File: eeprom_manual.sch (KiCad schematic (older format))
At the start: 45 parts, among them J1 Barrel_Jack, J2 Conn_01x02, SW1 SW_SPST, SW2 SW_DIP_x08, SW3 SW_DIP_x10, SW4 SW_DIP_x01, U1 74HC245, U2 L7805, U4 M54513FP, U5 28C16

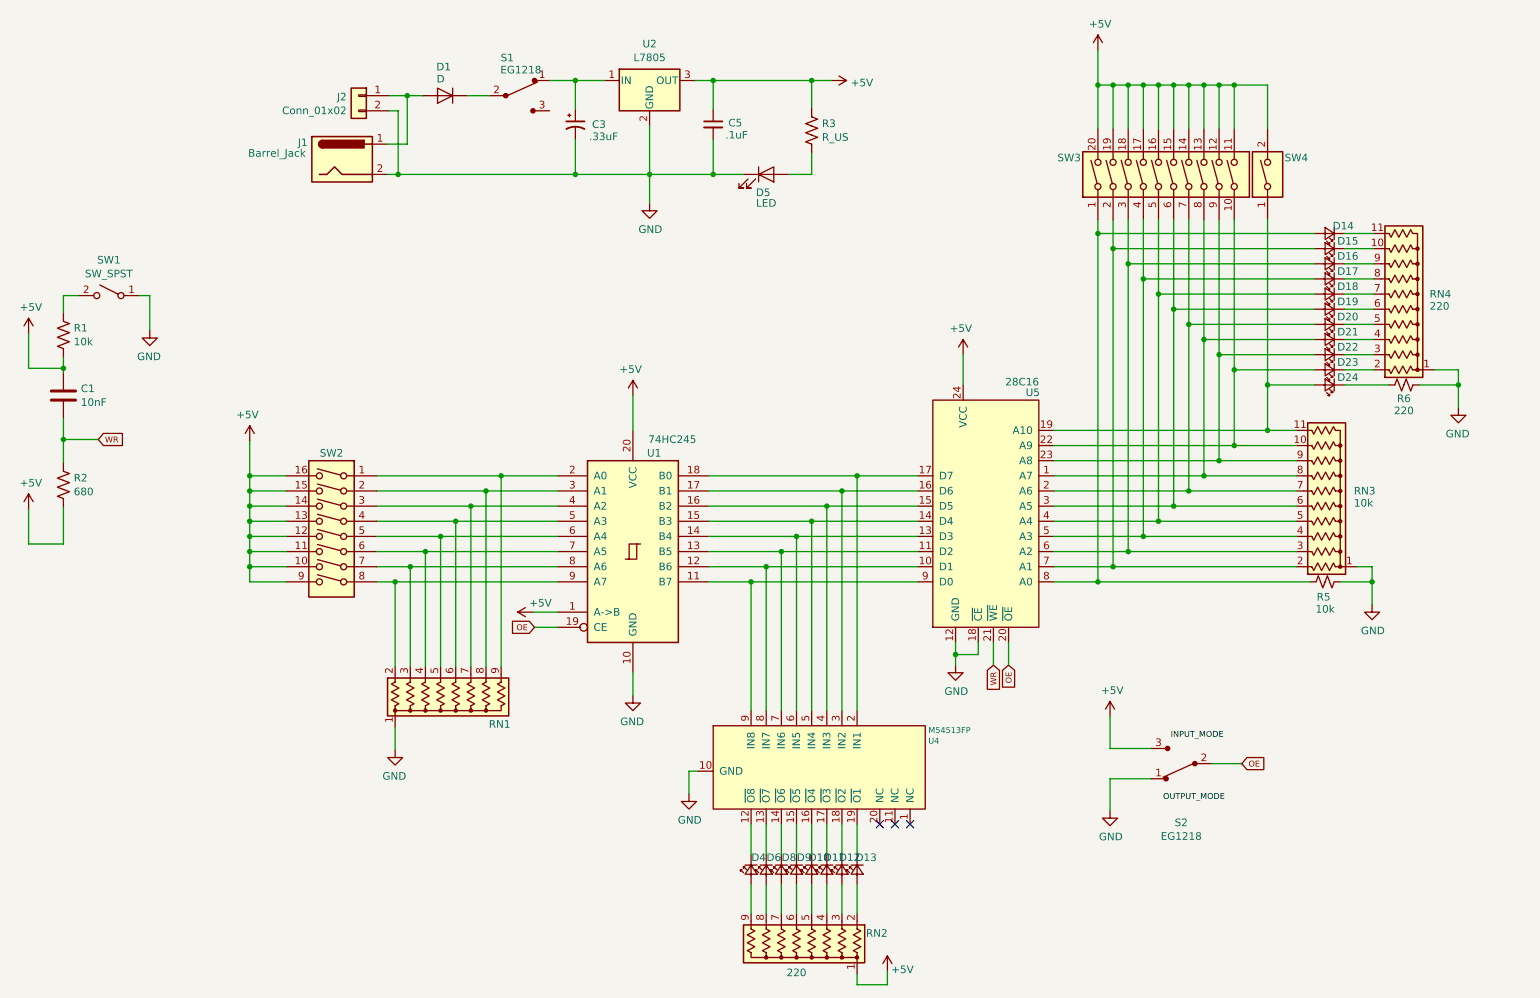
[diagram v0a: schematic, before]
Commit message: Assign footprints (initial)
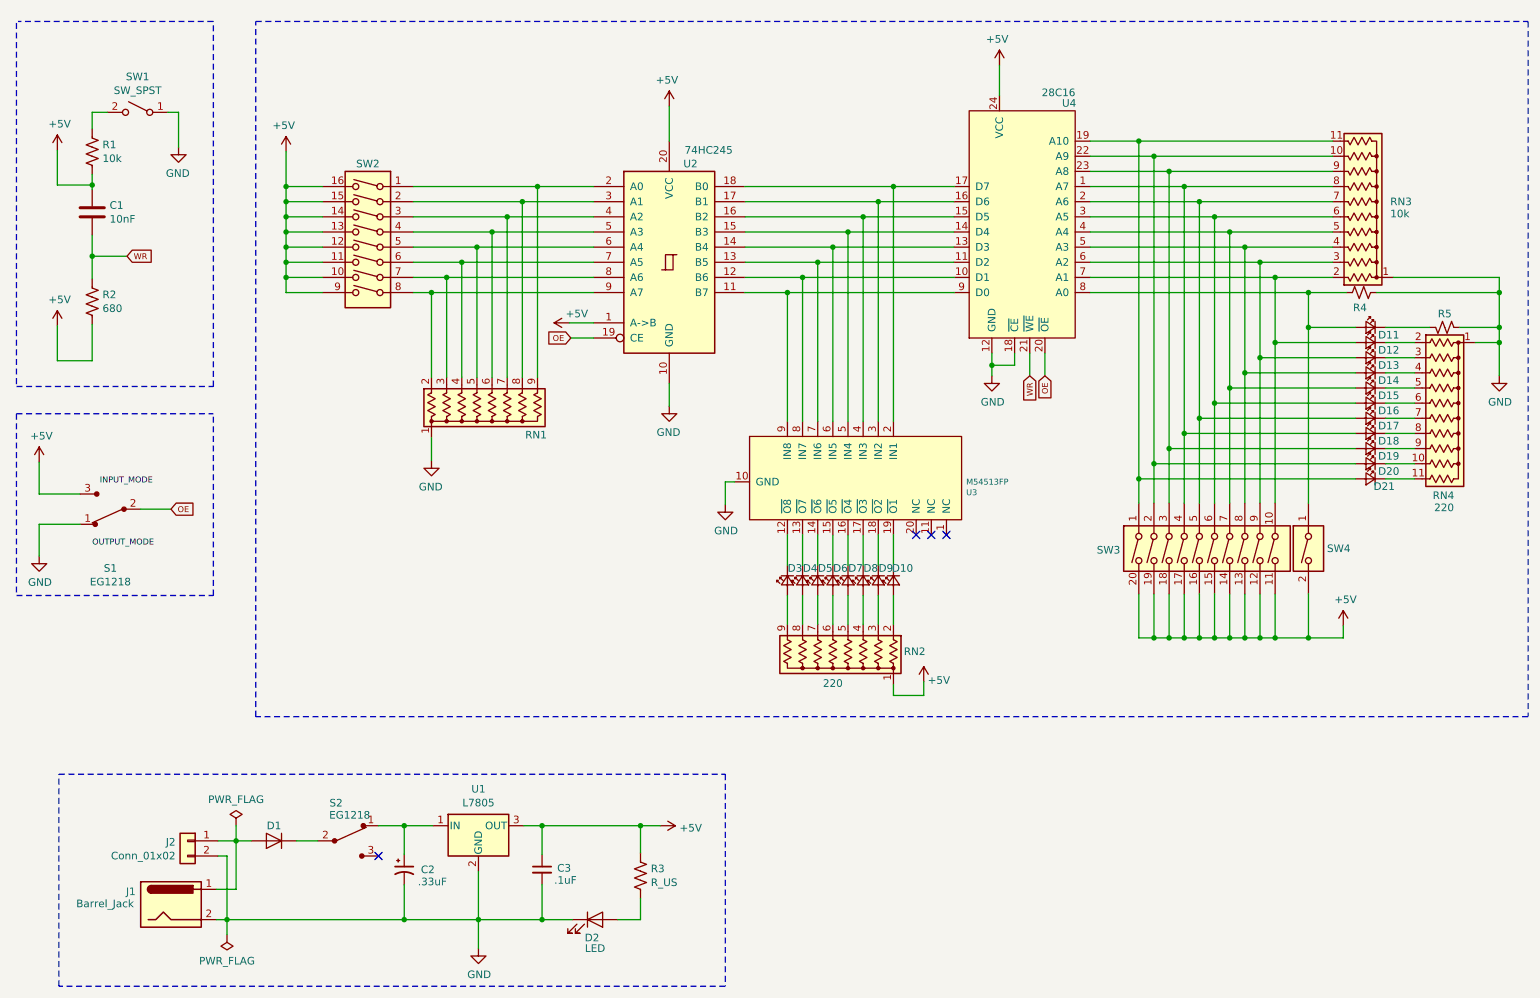
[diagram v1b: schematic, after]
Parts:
- C1: footprint (none) -> Capacitor_SMD:C_0805_2012Metric_Pad1.15x1.40mm_HandSolder
- C2: renamed from C3; footprint (none) -> Capacitor_SMD:C_0805_2012Metric_Pad1.15x1.40mm_HandSolder
- C3: renamed from C5; footprint (none) -> Capacitor_SMD:C_0805_2012Metric_Pad1.15x1.40mm_HandSolder
- D1: footprint (none) -> Diode_SMD:D_0805_2012Metric_Pad1.15x1.40mm_HandSolder
- D10: renamed from D13; footprint (none) -> LED_SMD:LED_0805_2012Metric_Pad1.15x1.40mm_HandSolder
- D11: renamed from D24; footprint (none) -> LED_SMD:LED_0805_2012Metric_Pad1.15x1.40mm_HandSolder
- D12: renamed from D23; footprint (none) -> LED_SMD:LED_0805_2012Metric_Pad1.15x1.40mm_HandSolder
- D13: renamed from D22; footprint (none) -> LED_SMD:LED_0805_2012Metric_Pad1.15x1.40mm_HandSolder
- D14: renamed from D21; footprint (none) -> LED_SMD:LED_0805_2012Metric_Pad1.15x1.40mm_HandSolder
- D15: renamed from D20; footprint (none) -> LED_SMD:LED_0805_2012Metric_Pad1.15x1.40mm_HandSolder
- D16: renamed from D19; footprint (none) -> LED_SMD:LED_0805_2012Metric_Pad1.15x1.40mm_HandSolder
- D17: renamed from D18; footprint (none) -> LED_SMD:LED_0805_2012Metric_Pad1.15x1.40mm_HandSolder
- D18: renamed from D17; footprint (none) -> LED_SMD:LED_0805_2012Metric_Pad1.15x1.40mm_HandSolder
- D19: renamed from D16; footprint (none) -> LED_SMD:LED_0805_2012Metric_Pad1.15x1.40mm_HandSolder
- D2: renamed from D5; footprint (none) -> LED_SMD:LED_0805_2012Metric_Pad1.15x1.40mm_HandSolder
- D20: renamed from D15; footprint (none) -> LED_SMD:LED_0805_2012Metric_Pad1.15x1.40mm_HandSolder
- D21: renamed from D14; footprint (none) -> LED_SMD:LED_0805_2012Metric_Pad1.15x1.40mm_HandSolder
- D3: renamed from D4; footprint (none) -> LED_SMD:LED_0805_2012Metric_Pad1.15x1.40mm_HandSolder
- D4: renamed from D6; footprint (none) -> LED_SMD:LED_0805_2012Metric_Pad1.15x1.40mm_HandSolder
- D5: renamed from D8; footprint (none) -> LED_SMD:LED_0805_2012Metric_Pad1.15x1.40mm_HandSolder
- D6: renamed from D9; footprint (none) -> LED_SMD:LED_0805_2012Metric_Pad1.15x1.40mm_HandSolder
- D7: renamed from D10; footprint (none) -> LED_SMD:LED_0805_2012Metric_Pad1.15x1.40mm_HandSolder
- D8: renamed from D11; footprint (none) -> LED_SMD:LED_0805_2012Metric_Pad1.15x1.40mm_HandSolder
- D9: renamed from D12; footprint (none) -> LED_SMD:LED_0805_2012Metric_Pad1.15x1.40mm_HandSolder
- J1: footprint (none) -> digikey-footprints:Barrel_Jack_5.5mmODx2.1mmID_PJ-202A
- J2: footprint (none) -> TerminalBlock:TerminalBlock_bornier-2_P5.08mm
- R1, R2, R3: footprint (none) -> Resistor_SMD:R_0805_2012Metric_Pad1.15x1.40mm_HandSolder
- R4: renamed from R5; footprint (none) -> Resistor_SMD:R_0805_2012Metric_Pad1.15x1.40mm_HandSolder
- R5: renamed from R6; footprint (none) -> Resistor_SMD:R_0805_2012Metric_Pad1.15x1.40mm_HandSolder
- SW1: footprint (none) -> Button_Switch_THT:SW_PUSH_6mm
- SW2: footprint (none) -> Button_Switch_THT:SW_DIP_SPSTx08_Slide_9.78x22.5mm_W7.62mm_P2.54mm
- SW3: footprint (none) -> Button_Switch_THT:SW_DIP_SPSTx10_Slide_9.78x27.58mm_W7.62mm_P2.54mm
- SW4: footprint (none) -> Button_Switch_THT:SW_DIP_SPSTx01_Slide_9.78x4.72mm_W7.62mm_P2.54mm
- U1: renamed from U2; footprint (none) -> Package_TO_SOT_THT:TO-220-3_Horizontal_TabDown
- U2: renamed from U1; footprint (none) -> Package_DIP:DIP-20_W7.62mm_Socket
- U3: renamed from U4; footprint (none) -> digikey-footprints:SSOP-20_W3.9mm
- U4: renamed from U5; footprint (none) -> Socket:DIP_Socket-24_W11.9_W12.7_W15.24_W17.78_W18.5_3M_224-1275-00-0602J
- renumbered S2 to S1, S1 to S2
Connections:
- net at RN3.8 (R7), U4.1 (A7): now also D18.2 (A), SW3.4; no longer D14.2 (A), SW3.8
- net at RN3.11 (R10), U4.19 (A10): now also D21.2 (A), SW3.1; no longer D11.2 (A), SW4.1
- net at RN3.7 (R6), U4.2 (A6): now also D17.2 (A), SW3.5; no longer D15.2 (A), SW3.7
- net at RN3.10 (R9), U4.22 (A9): now also D20.2 (A), SW3.2; no longer D12.2 (A), SW3.10
- net at RN3.9 (R8), U4.23 (A8): now also D19.2 (A), SW3.3; no longer D13.2 (A), SW3.9
- net at RN3.5 (R4), U4.4 (A4): now also D15.2 (A), SW3.7; no longer D17.2 (A), SW3.5
- net at RN3.4 (R3), U4.5 (A3): now also D14.2 (A), SW3.8; no longer D18.2 (A), SW3.4
- net at RN3.3 (R2), U4.6 (A2): now also D13.2 (A), SW3.9; no longer D19.2 (A), SW3.3
- net at RN3.2 (R1), U4.7 (A1): now also D12.2 (A), SW3.10; no longer D20.2 (A), SW3.2
- net at R4.2, U4.8 (A0): now also D11.2 (A), SW4.1; no longer D21.2 (A), SW3.1
- no-connect marks 3 -> 4
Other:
- moved on the sheet: C1, C2, C3, D1, D10, D11, D12, D13, D14, D15, D16, D17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

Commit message: Update footprints
- Generate net list
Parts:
- U2: footprint Package_DIP:DIP-20_W7.62mm_Socket -> Package_SO:TSSOP-20_4.4x6.5mm_P0.65mm
- U3: footprint digikey-footprints:SSOP-20_W3.9mm -> digikey-footprints:SSOP-20_W5.3mm
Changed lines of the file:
@@
 F 0 "U2" H 5340 3120 50  0000 C CNN
 F 1 "74HC245" H 5460 3210 50  0000 C CNN
-F 2 "Package_DIP:DIP-20_W7.62mm_Socket" H 5200 2470 50  0001 C CNN
+F 2 "Package_SO:TSSOP-20_4.4x6.5mm_P0.65mm" H 5200 2470 50  0001 C CNN
 F 3 "http://www.ti.com/lit/gpn/sn74HC245" H 5200 2470 50  0001 C CNN
 	1    5200 2470
@@
 F 0 "U3" V 6500 4650 39  0000 L CNN
 F 1 "M54513FP" V 6430 4650 39  0000 L CNN
-F 2 "digikey-footprints:SSOP-20_W3.9mm" H 6230 3620 39  0001 C CNN
+F 2 "digikey-footprints:SSOP-20_W5.3mm" H 6230 3620 39  0001 C CNN
 F 3 "" H 6230 3620 39  0001 C CNN
 	1    6430 3920
